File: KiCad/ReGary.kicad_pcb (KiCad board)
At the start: 4 copper layers, 38 x 38 mm, 37 parts, among them U1 GW1N-UV1P5LQ100, U2 LM1117-3.3, U3 SN74CBT16210, U4 SN74CBT16210, U5 SN74CBT16210, U6 SN74CBT16210, U7 PLCC_84_plug, U8 PLCC_84_plug, U9 TPS73643DBV

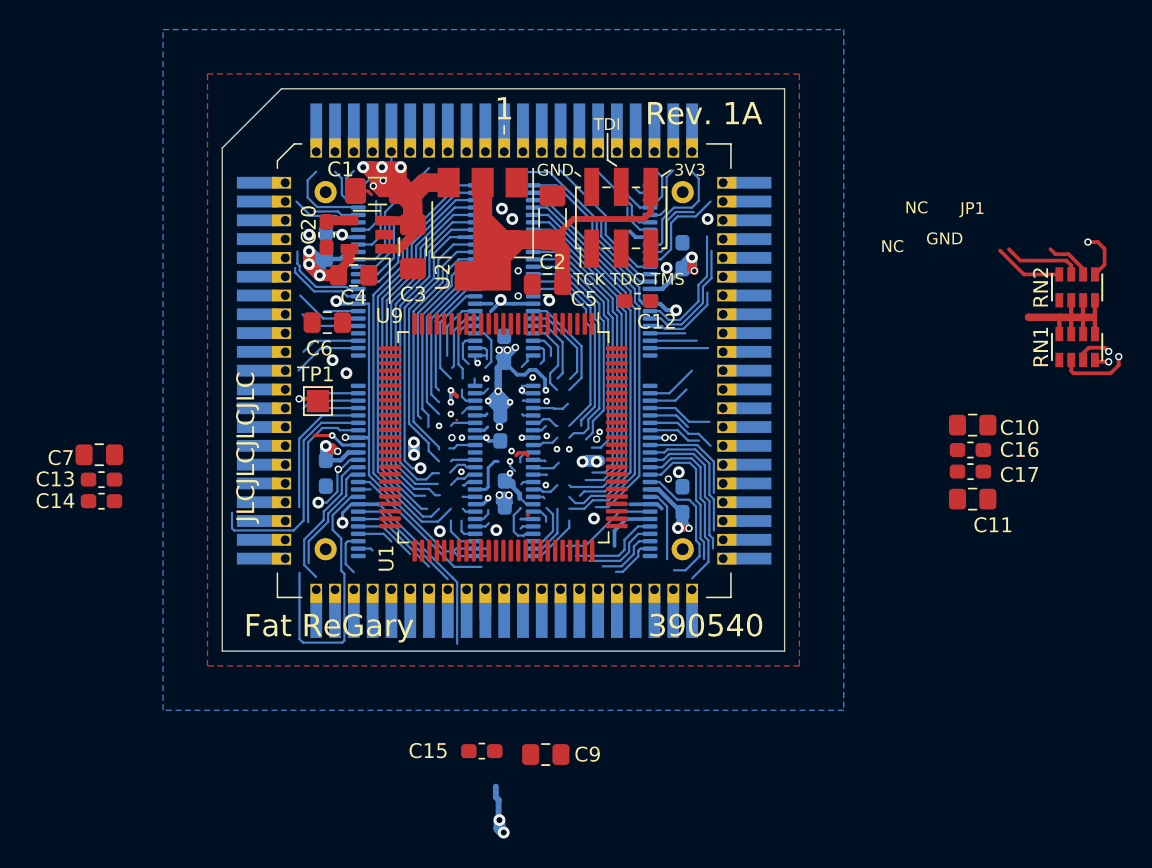
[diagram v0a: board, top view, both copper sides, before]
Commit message: fixed placement of capacitors C8 and C9
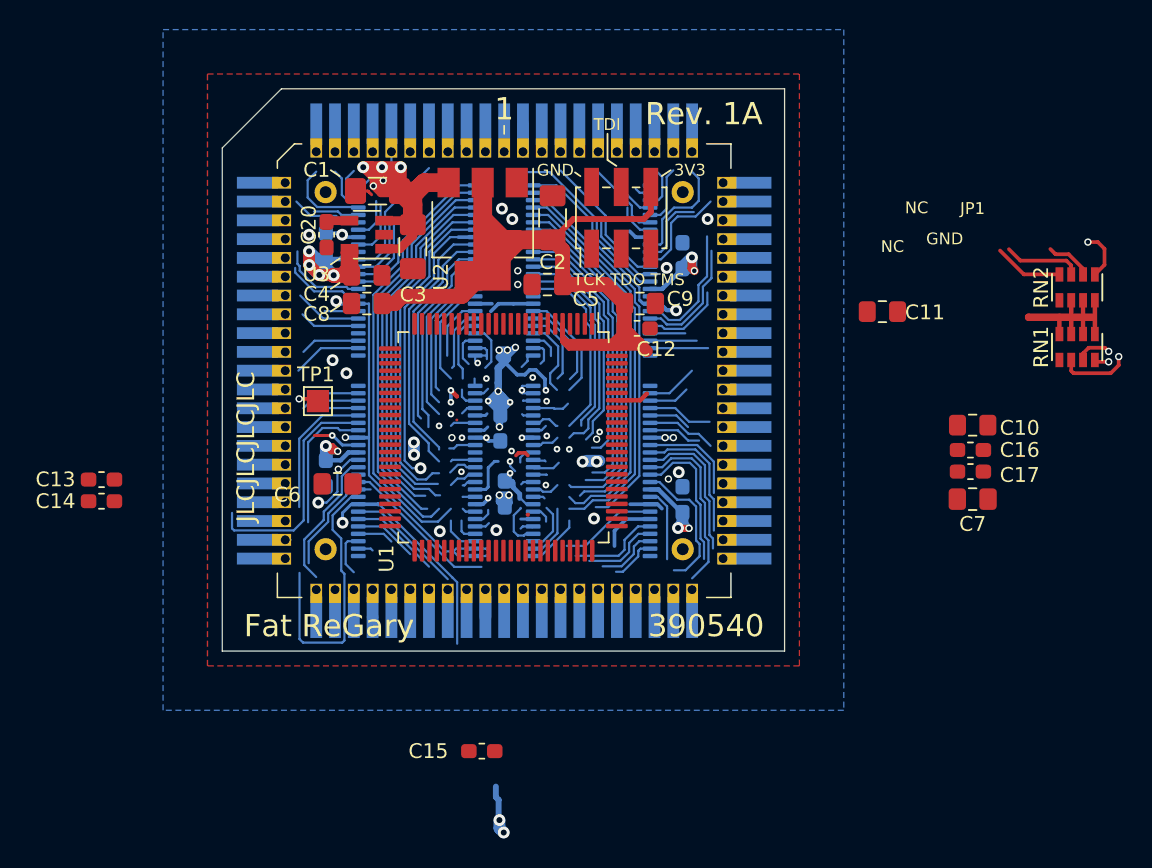
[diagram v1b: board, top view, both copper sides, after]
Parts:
- removed the C7 at (117.1, 80.1)
- removed the U9 at (135.2, 65.3)
- added C11: 0.1uF, Capacitor_SMD:C_0805_2012Metric_Pad1.15x1.40mm_HandSolder, F.Cu at (170.0, 70.5)
- added U3: TPS73643DBV, Package_TO_SOT_SMD:SOT-23-5, F.Cu at (135.2, 65.3)
- C5, C6, C9: footprint Capacitor_SMD:C_0805_2012Metric_Pad1.15x1.40mm_HandSolder -> Capacitor_SMD:C_0805_2012Metric_Pad1.18x1.45mm_HandSolder
- C7: renamed from C11; footprint Capacitor_SMD:C_0805_2012Metric_Pad1.15x1.40mm_HandSolder -> Capacitor_SMD:C_0805_2012Metric_Pad1.18x1.45mm_HandSolder
- C8: footprint Capacitor_SMD:C_0603_1608Metric_Pad1.05x0.95mm_HandSolder -> Capacitor_SMD:C_0805_2012Metric_Pad1.18x1.45mm_HandSolder; moved to F.Cu
- moved C9 31.1 mm to (153.6, 69.9)
- moved C6 10.9 mm to (133.2, 82.1)
- moved C8 9.78 mm to (135.2, 69.9), turned to 0 degrees
- moved C12 1.84 mm to (153.4, 71.6)
- moved C4 0.89 mm to (135.2, 68.0)
- renumbered U3 to U4, U4 to U5, U5 to U6, U6 to U7, U7 to U8, U8 to U9
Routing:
- net 3V3: track 76.9 -> 119.6 mm
- net 4V3: track 37.1 -> 41.8 mm, vias 9 -> 10
- net GND: vias 45 -> 43

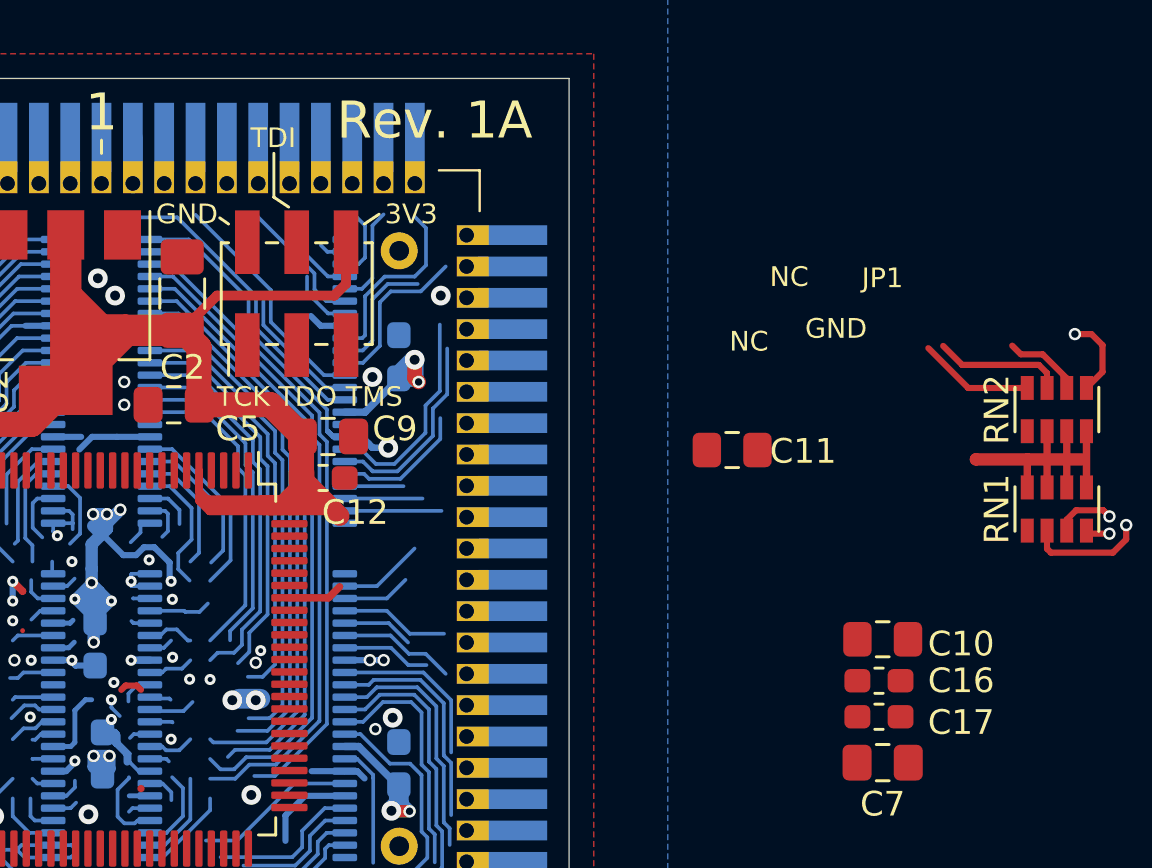
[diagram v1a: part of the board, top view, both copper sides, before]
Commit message: Add JTAG routing and 4.7k pull-down resistor on TCK-line
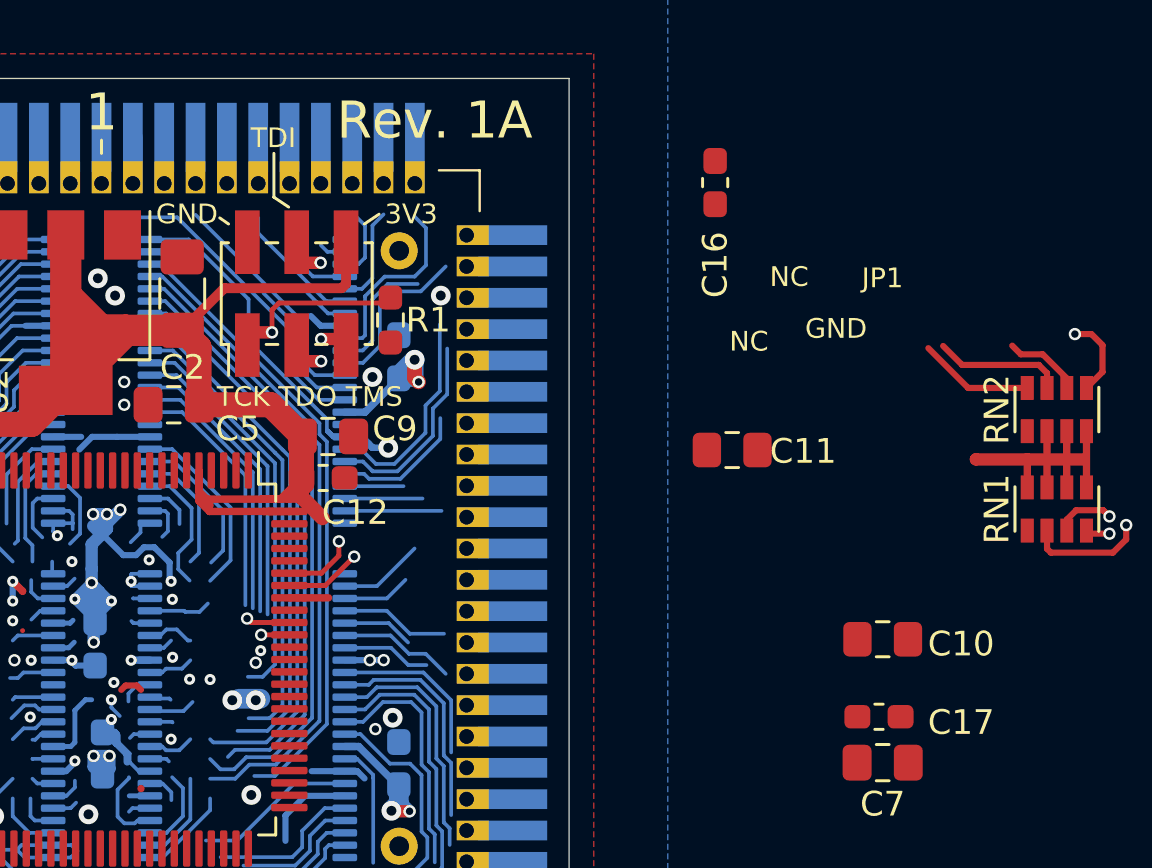
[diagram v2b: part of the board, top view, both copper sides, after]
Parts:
- added R1: 4k7, Resistor_SMD:R_0603_1608Metric_Pad0.98x0.95mm_HandSolder, F.Cu at (156.2, 65.2)
- moved C16 21.3 mm to (169.3, 59.6), turned to 90 degrees
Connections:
- C11 pad 1: GND -> Net-(C11-Pad1)
- C11 pad 2: 3V3 -> Net-(C11-Pad2)
- RN2 pad 1: TDI -> Net-(RN2-Pad1)
- RN2 pad 3: TMS -> Net-(RN2-Pad3)
- U1 pad 90: Net-(U1-Pad90) -> TMS
- U1 pad 91: Net-(U1-Pad91) -> TCK
- U1 pad 94: Net-(U1-Pad94) -> TDI
- U1 pad 95: Net-(U1-Pad95) -> TDO
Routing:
- net TCK: track 11.4 -> 32.5 mm, vias 0 -> 2
- net nCONFIG: track 12.8 -> 0.80 mm
- net nSTATUS: track 15.8 -> 4.81 mm
- net TMS: track 7.53 -> 17.5 mm, vias 0 -> 2
- net JP1: track 13.1 -> 3.15 mm
- net CONF_DONE: track 11.9 -> 2.44 mm
- net 3V3: track 119.6 -> 110.4 mm
- net TDO: track 13.5 -> 22.3 mm, vias 0 -> 2
- net Net-(RN2-Pad3): track 0.00 -> 5.27 mm
- net BINT_FPGA: track 15.3 -> 11.6 mm
- net Net-(RN2-Pad1): track 0.00 -> 3.31 mm, vias 0 -> 1
- net EBG1_FPGA: track 15.3 -> 12.3 mm
- net FCS_FPGA: track 12.7 -> 10.2 mm
- net EDS1_FPGA: track 13.1 -> 10.9 mm
- net TDI: track 18.0 -> 17.2 mm, vias 1 -> 2
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
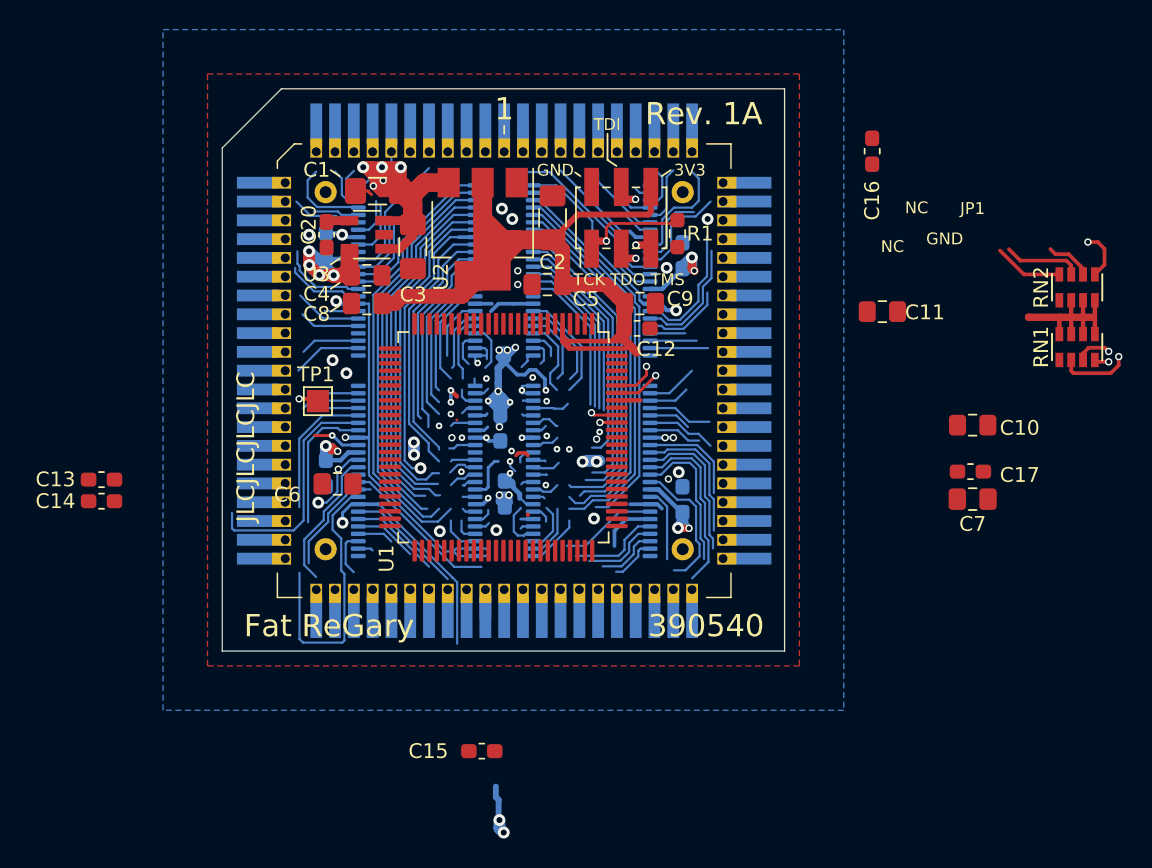
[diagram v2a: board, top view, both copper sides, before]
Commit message: fixed placement of capacitors C9,C10 and resistor array RN1
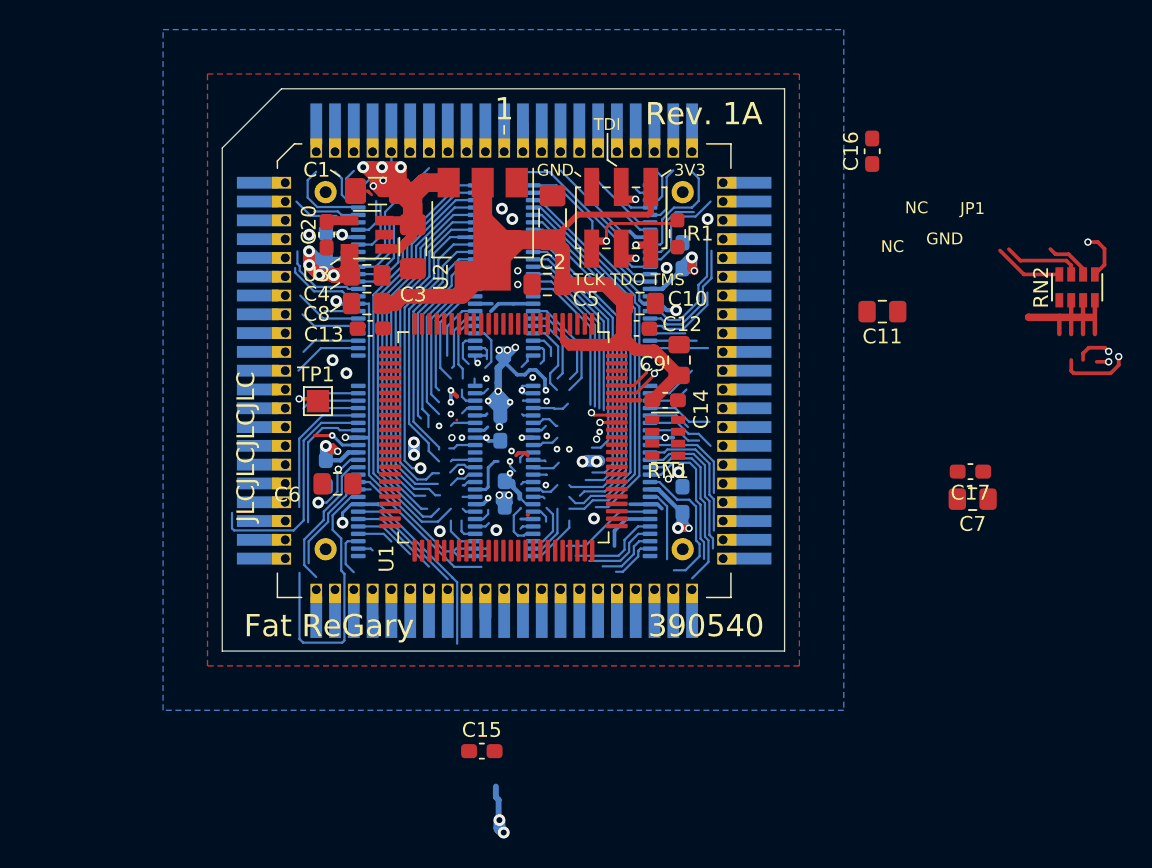
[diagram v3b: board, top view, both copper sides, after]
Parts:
- C10, C11: footprint Capacitor_SMD:C_0805_2012Metric_Pad1.15x1.40mm_HandSolder -> Capacitor_SMD:C_0805_2012Metric_Pad1.18x1.45mm_HandSolder
- C12, C13, C14, C15, C16, C17, C18, C19: footprint Capacitor_SMD:C_0603_1608Metric_Pad1.05x0.95mm_HandSolder -> Capacitor_SMD:C_0603_1608Metric_Pad1.08x0.95mm_HandSolder
- moved C14 38.7 mm to (155.3, 76.5), turned to 180 degrees
- moved RN1 28.5 mm to (155.3, 79.0), turned to 0 degrees
- moved C10 23.9 mm to (153.6, 69.9)
- moved C13 20.8 mm to (135.4, 71.6)
- moved C9 4.64 mm to (156.3, 73.7), turned to 270 degrees
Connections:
- C11 pad 1: Net-(C11-Pad1) -> GND
- C11 pad 2: Net-(C11-Pad2) -> 3V3
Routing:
- net 3V3: track 110.4 -> 126.5 mm
- net TDI: track 17.2 -> 6.72 mm
- net GND: vias 43 -> 42

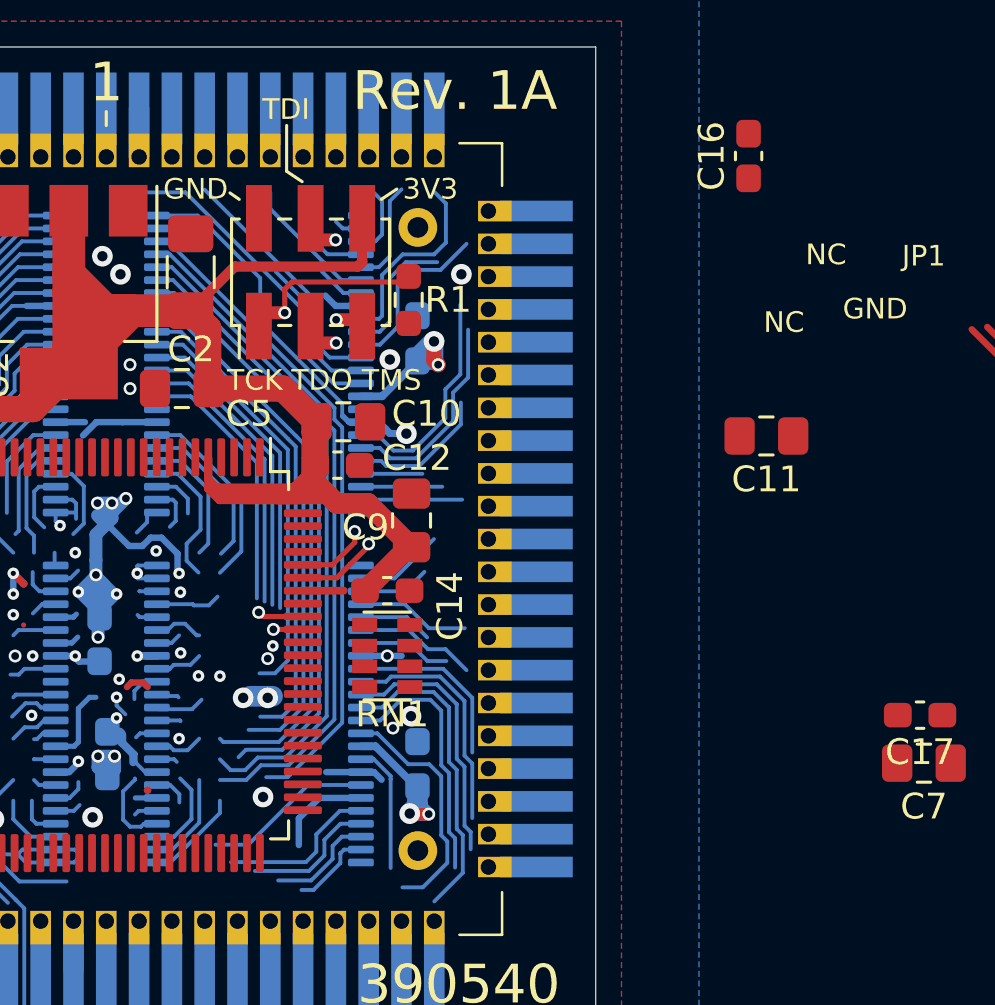
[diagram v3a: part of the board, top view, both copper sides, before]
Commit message: Add JP header for JTAGSEL_N, fixed JTAG as dual-purpose pins
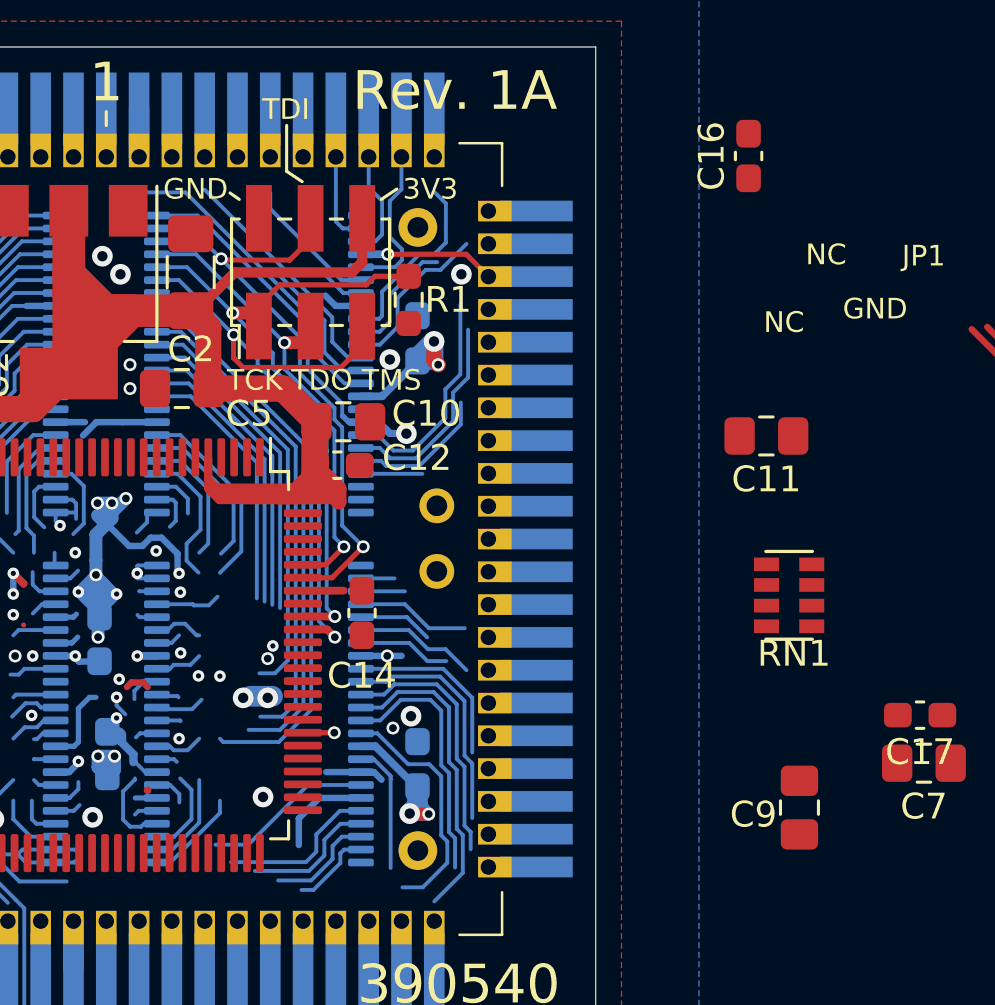
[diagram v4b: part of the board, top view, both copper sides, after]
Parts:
- added J1: Conn_01x02, Connector_PinHeader_2.00mm:PinHeader_1x02_P2.00mm_Vertical, F.Cu at (157.2, 75.5)
- moved C9 18.7 mm to (171.3, 84.9)
- moved RN1 15.7 mm to (170.9, 76.6)
- moved C14 1.31 mm to (154.3, 77.3), turned to 90 degrees
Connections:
- net CONF_DONE renamed Net-(RN1-Pad3)
- net Net-(U1-Pad81) renamed RECONFIG_N
- net nCONFIG renamed Net-(RN1-Pad4)
- net nSTATUS renamed Net-(RN1-Pad2)
- JTAG1 pad 1: TCK -> LADR_TCK_FPGA
- JTAG1 pad 3: TDO -> LMDS_TDO_FPGA
- JTAG1 pad 4: TDI -> UMDS_TDI_FPGA
- JTAG1 pad 5: TMS -> LLDS_TMS_FPGA
- R1 pad 2: TCK -> LADR_TCK_FPGA
- RN1 pad 1: Net-(RN1-Pad1) -> JTAGSEL_N
- U1 pad 82: Net-(U1-Pad82) -> JTAGSEL_N
- U1 pad 90: TMS -> LLDS_TMS_FPGA
- U1 pad 91: TCK -> LADR_TCK_FPGA
- U1 pad 94: TDI -> UMDS_TDI_FPGA
- U1 pad 95: TDO -> LMDS_TDO_FPGA
- U4 pad 2: EBR2 -> UMDS
- U4 pad 3: EBR3 -> LMDS
- U4 pad 4: EBR1 -> LADR
- U4 pad 43: EBR4_FPGA -> LLDS_TMS_FPGA
- U4 pad 44: EBR1_FPGA -> LADR_TCK_FPGA
- U4 pad 45: EBR3_FPGA -> LMDS_TDO_FPGA
- U4 pad 46: EBR2_FPGA -> UMDS_TDI_FPGA
- U4 pad 5: EBR4 -> LLDS
- U8 pad 72: Net-(U8-Pad72) -> LADR
- U8 pad 76: Net-(U8-Pad76) -> LLDS
- U8 pad 77: Net-(U8-Pad77) -> LMDS
- U8 pad 78: Net-(U8-Pad78) -> UMDS
- U8 pad 79: Net-(U8-Pad79) -> UUDS
- U9 pad 72: Net-(U9-Pad72) -> LADR
- U9 pad 76: Net-(U9-Pad76) -> LLDS
- U9 pad 77: Net-(U9-Pad77) -> LMDS
- U9 pad 78: Net-(U9-Pad78) -> UMDS
- U9 pad 79: Net-(U9-Pad79) -> UUDS
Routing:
- net LADR_TCK_FPGA: track 0.00 -> 26.9 mm, vias 0 -> 2
- net EBR3_FPGA: track 26.6 -> 0.00 mm
- net LLDS_TMS_FPGA: track 0.00 -> 25.7 mm, vias 0 -> 2
- net EBR2_FPGA: track 25.7 -> 0.00 mm
- net EBR1_FPGA: track 25.6 -> 0.00 mm
- net UMDS_TDI_FPGA: track 0.00 -> 23.7 mm, vias 0 -> 2
- net EBR4_FPGA: track 23.6 -> 0.00 mm
- net LMDS_TDO_FPGA: track 0.00 -> 19.1 mm, vias 0 -> 2
- net TCK: track 32.5 -> 13.7 mm, vias 2 -> 0
- net TMS: track 17.5 -> 2.26 mm, vias 2 -> 0
- net TDO: track 22.2 -> 10.3 mm, vias 2 -> 0
- net JTAGSEL_N: track 0.00 -> 9.56 mm, vias 0 -> 1
- net EBR0_FPGA: track 23.1 -> 15.4 mm
- net TDI: track 6.72 -> 0.00 mm, vias 2 -> 0
- net LLDS: track 0.00 -> 6.08 mm
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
